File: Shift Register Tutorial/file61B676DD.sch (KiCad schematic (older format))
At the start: 7 parts, among them Q301 2N3904, SW301 SW_Push

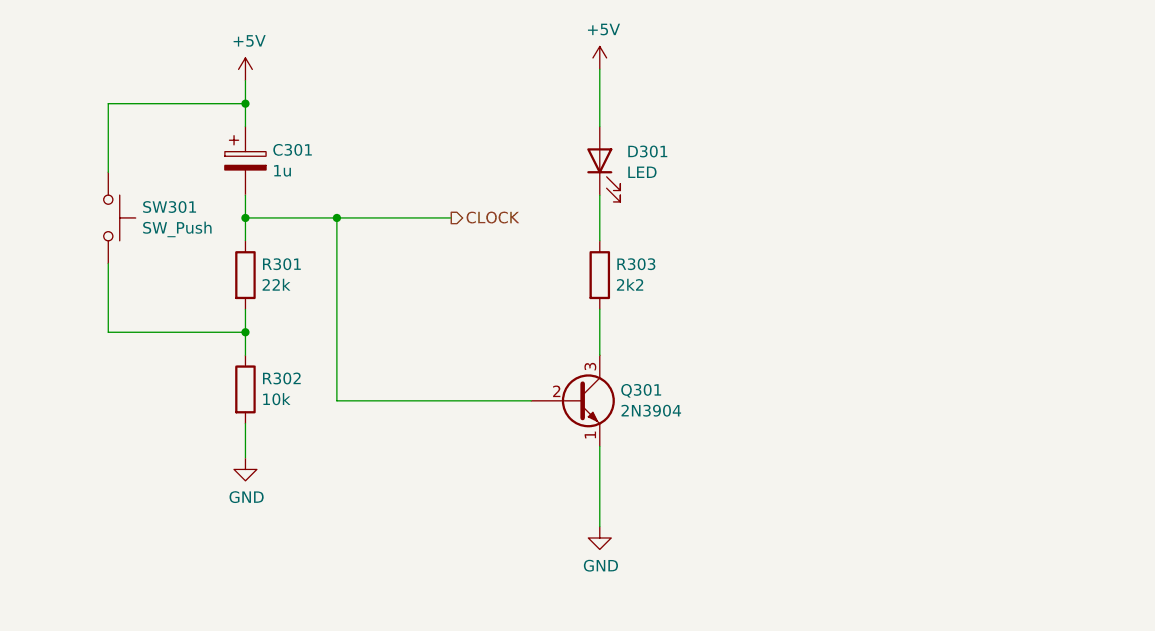
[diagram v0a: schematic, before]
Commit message: Fix shift register tutorial (#11)
I had forgotten how NPN transistors worked, which resulted in the push buttons not affecting their target pins. Remove the transistors & indicator LEDs, and shrink the board.
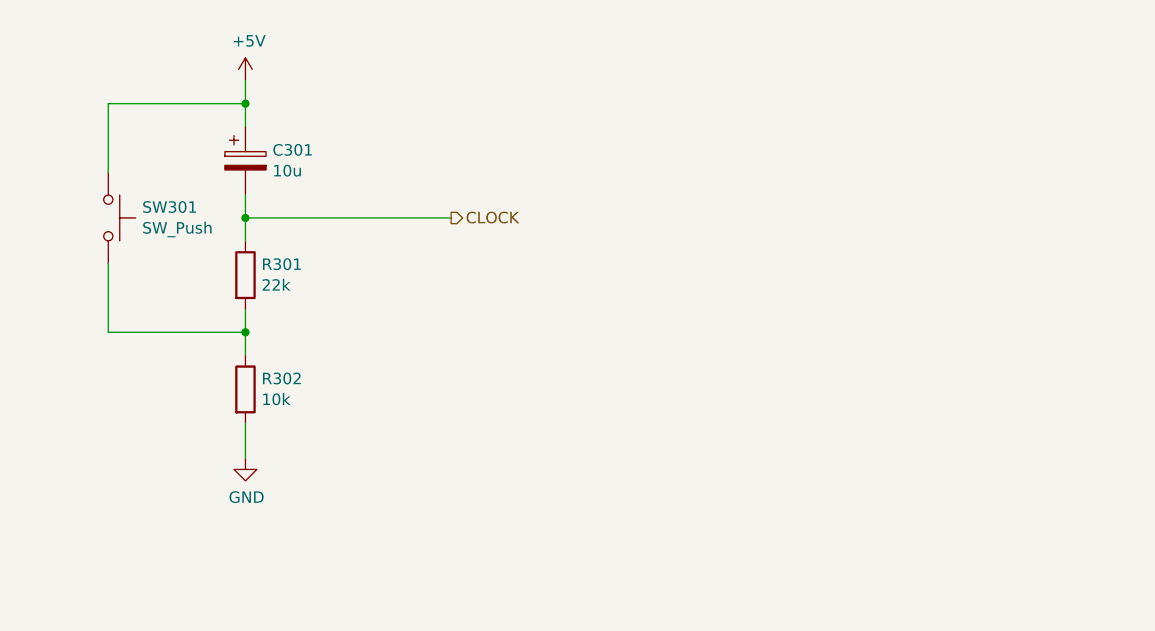
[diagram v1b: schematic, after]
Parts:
- removed D301: LED, LED_THT:LED_D5.0mm, symbol Device:LED
- removed Q301: 2N3904, Package_TO_SOT_THT:TO-92_Inline_Wide, symbol Transistor_BJT:2N3904
- removed R303: 2k2, Resistor_THT:R_Axial_DIN0207_L6.3mm_D2.5mm_P7.62mm_Horizontal, symbol Device:R
- C301: value 1u -> 10u
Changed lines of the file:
@@
 AR Path="/61B676DE/61B6A311" Ref="C301"  Part="1"
 F 0 "C301" H 2768 1746 50  0000 L CNN
-F 1 "1u" H 2768 1655 50  0000 L CNN
+F 1 "10u" H 2768 1655 50  0000 L CNN
 F 2 "Capacitor_THT:CP_Radial_D4.0mm_P2.00mm" H 2688 1550 50  0001 C CNN
 F 3 "~" H 2650 1700 50  0001 C CNN
@@
 Text HLabel 3550 1950 2    50   Output ~ 0
 CLOCK
-Wire Wire Line
-	2650 1950 3050 1950
 Connection ~ 2650 1950
 Wire Wire Line
 	2650 1950 2650 2050
-$Comp
-L Transistor_BJT:2N3904 Q?
-U 1 1 61B6A339
-P 4100 2750
-AR Path="/61B52EB5/61B6A339" Ref="Q?"  Part="1"
-AR Path="/61B676DE/61B6A339" Ref="Q301"  Part="1"
-F 0 "Q301" H 4290 2796 50  0000 L CNN
-F 1 "2N3904" H 4290 2705 50  0000 L CNN
-F 2 "Package_TO_SOT_THT:TO-92_Inline_Wide" H 4300 2675 50  0001 L CIN
-F 3 "https://www.onsemi.com/pub/Collateral/2N3903-D.PDF" H 4100 2750 50  0001 L CNN
-	1    4100 2750
-	1    0    0    -1
-$EndComp
 Wire Wire Line
-	3050 1950 3050 2750
-Wire Wire Line
-	3050 2750 3900 2750
-Connection ~ 3050 1950
-Wire Wire Line
-	3050 1950 3550 1950
-$Comp
-L power:GND #PWR?
-U 1 1 61B6A343
-P 4200 3300
-AR Path="/61B52EB5/61B6A343" Ref="#PWR?"  Part="1"
-AR Path="/61B676DE/61B6A343" Ref="#PWR0304"  Part="1"
-F 0 "#PWR0304" H 4200 3050 50  0001 C CNN
-F 1 "GND" H 4205 3127 50  0000 C CNN
-F 2 "" H 4200 3300 50  0001 C CNN
-F 3 "" H 4200 3300 50  0001 C CNN
-	1    4200 3300
-	1    0    0    -1
-$EndComp
-Wire Wire Line
-	4200 2950 4200 3300
-$Comp
-L Device:R R?
-U 1 1 61B6A34A
-P 4200 2200
-AR Path="/61B52EB5/61B6A34A" Ref="R?"  Part="1"
-AR Path="/61B676DE/61B6A34A" Ref="R303"  Part="1"
-F 0 "R303" H 4270 2246 50  0000 L CNN
-F 1 "2k2" H 4270 2155 50  0000 L CNN
-F 2 "Resistor_THT:R_Axial_DIN0207_L6.3mm_D2.5mm_P7.62mm_Horizontal" V 4130 2200 50  0001 C CNN
-F 3 "~" H 4200 2200 50  0001 C CNN
-	1    4200 2200
-	1    0    0    -1
-$EndComp
-$Comp
-L Device:LED D?
-U 1 1 61B6A350
-P 4200 1700
-AR Path="/61B52EB5/61B6A350" Ref="D?"  Part="1"
-AR Path="/61B676DE/61B6A350" Ref="D301"  Part="1"
-F 0 "D301" V 4239 1582 50  0000 R CNN
-F 1 "LED" V 4148 1582 50  0000 R CNN
-F 2 "LED_THT:LED_D5.0mm" H 4200 1700 50  0001 C CNN
-F 3 "~" H 4200 1700 50  0001 C CNN
-	1    4200 1700
-	0    -1   -1   0
-$EndComp
-$Comp
-L power:+5V #PWR?
-U 1 1 61B6A356
-P 4200 1300
-AR Path="/61B52EB5/61B6A356" Ref="#PWR?"  Part="1"
-AR Path="/61B676DE/61B6A356" Ref="#PWR0303"  Part="1"
-F 0 "#PWR0303" H 4200 1150 50  0001 C CNN
-F 1 "+5V" H 4215 1473 50  0000 C CNN
-F 2 "" H 4200 1300 50  0001 C CNN
-F 3 "" H 4200 1300 50  0001 C CNN
-	1    4200 1300
-	1    0    0    -1
-$EndComp
-Wire Wire Line
-	4200 1300 4200 1550
-Wire Wire Line
-	4200 1850 4200 2050
-Wire Wire Line
-	4200 2350 4200 2550
+	2650 1950 3550 1950
 $EndSCHEMATC

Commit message: Another attempt at the Shift Registers (#12)
It appears that clock pins are very finicky about debouncing. Switch to using a 555 monostable for this purpose, and remove debounce from the other pins. The 'data' pin only matters on the clock edge, and the 'reset' pin is idempotent.
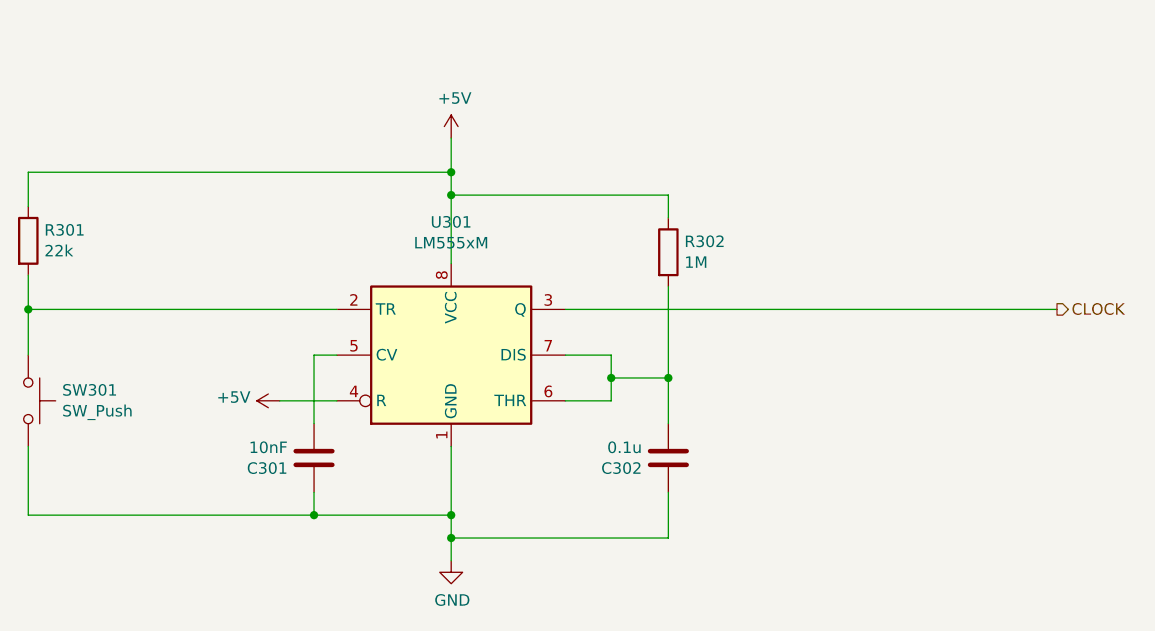
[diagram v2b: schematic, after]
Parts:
- removed C301: 10u, Capacitor_THT:CP_Radial_D4.0mm_P2.00mm, symbol Device:CP
- added C301: 10nF, Capacitor_THT:C_Disc_D3.0mm_W2.0mm_P2.50mm, symbol Device:C
- added C302: 0.1u, Capacitor_THT:C_Disc_D4.7mm_W2.5mm_P5.00mm, symbol Device:C
- added U301: LM555xM, Package_DIP:DIP-8_W7.62mm_Socket, symbol Timer:LM555xM
- R302: value 10k -> 1M
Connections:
- net +5V: now also R301.1, R302.1, U301.4 (R), U301.8 (VCC); no longer SW301.1
- net CLOCK: now also U301.3 (Q); no longer R301.1
- net GND: now also SW301.2, C301.2, C302.1, U301.1 (GND); no longer R302.2
- new net: R301.2, SW301.1, U301.2 (TR)
- new net: C301.1, U301.5 (CV)
- new net: C302.2, R302.2, U301.6 (THR), U301.7 (DIS)
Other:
- moved on the sheet: SW301
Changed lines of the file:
@@
 $EndDescr
-$Comp
-L Device:R R?
-U 1 1 61B6A305
-P 2650 2700
-AR Path="/61B52EB5/61B6A305" Ref="R?"  Part="1"
-AR Path="/61B676DE/61B6A305" Ref="R302"  Part="1"
-F 0 "R302" H 2720 2746 50  0000 L CNN
-F 1 "10k" H 2720 2655 50  0000 L CNN
-F 2 "Resistor_THT:R_Axial_DIN0207_L6.3mm_D2.5mm_P7.62mm_Horizontal" V 2580 2700 50  0001 C CNN
-F 3 "~" H 2650 2700 50  0001 C CNN
-	1    2650 2700
-	1    0    0    -1
-$EndComp
-$Comp
-L Device:R R?
-U 1 1 61B6A30B
-P 2650 2200
-AR Path="/61B52EB5/61B6A30B" Ref="R?"  Part="1"
-AR Path="/61B676DE/61B6A30B" Ref="R301"  Part="1"
-F 0 "R301" H 2720 2246 50  0000 L CNN
-F 1 "22k" H 2720 2155 50  0000 L CNN
-F 2 "Resistor_THT:R_Axial_DIN0207_L6.3mm_D2.5mm_P7.62mm_Horizontal" V 2580 2200 50  0001 C CNN
-F 3 "~" H 2650 2200 50  0001 C CNN
-	1    2650 2200
-	1    0    0    -1
-$EndComp
-$Comp
-L Device:CP C?
-U 1 1 61B6A311
-P 2650 1700
-AR Path="/61B52EB5/61B6A311" Ref="C?"  Part="1"
-AR Path="/61B676DE/61B6A311" Ref="C301"  Part="1"
-F 0 "C301" H 2768 1746 50  0000 L CNN
-F 1 "10u" H 2768 1655 50  0000 L CNN
-F 2 "Capacitor_THT:CP_Radial_D4.0mm_P2.00mm" H 2688 1550 50  0001 C CNN
-F 3 "~" H 2650 1700 50  0001 C CNN
-	1    2650 1700
-	1    0    0    -1
-$EndComp
 $Comp
 L power:+5V #PWR?
 U 1 1 61B6A317
-P 2650 1350
+P 3550 1600
 AR Path="/61B52EB5/61B6A317" Ref="#PWR?"  Part="1"
-AR Path="/61B676DE/61B6A317" Ref="#PWR0301"  Part="1"
-F 0 "#PWR0301" H 2650 1200 50  0001 C CNN
-F 1 "+5V" H 2665 1523 50  0000 C CNN
-F 2 "" H 2650 1350 50  0001 C CNN
-F 3 "" H 2650 1350 50  0001 C CNN
-	1    2650 1350
+AR Path="/61B676DE/61B6A317" Ref="#PWR0302"  Part="1"
+F 0 "#PWR0302" H 3550 1450 50  0001 C CNN
+F 1 "+5V" H 3565 1773 50  0000 C CNN
+F 2 "" H 3550 1600 50  0001 C CNN
+F 3 "" H 3550 1600 50  0001 C CNN
+	1    3550 1600
 	1    0    0    -1
 $EndComp
@@
 L power:GND #PWR?
 U 1 1 61B6A31D
-P 2650 3000
+P 3550 3450
 AR Path="/61B52EB5/61B6A31D" Ref="#PWR?"  Part="1"
-AR Path="/61B676DE/61B6A31D" Ref="#PWR0302"  Part="1"
-F 0 "#PWR0302" H 2650 2750 50  0001 C CNN
-F 1 "GND" H 2655 2827 50  0000 C CNN
-F 2 "" H 2650 3000 50  0001 C CNN
-F 3 "" H 2650 3000 50  0001 C CNN
-	1    2650 3000
+AR Path="/61B676DE/61B6A31D" Ref="#PWR0303"  Part="1"
+F 0 "#PWR0303" H 3550 3200 50  0001 C CNN
+F 1 "GND" H 3555 3277 50  0000 C CNN
+F 2 "" H 3550 3450 50  0001 C CNN
+F 3 "" H 3550 3450 50  0001 C CNN
+	1    3550 3450
+	1    0    0    -1
+$EndComp
+$Comp
+L Switch:SW_Push SW?
+U 1 1 61B6A327
+P 1700 2750
+AR Path="/61B52EB5/61B6A327" Ref="SW?"  Part="1"
+AR Path="/61B676DE/61B6A327" Ref="SW301"  Part="1"
+F 0 "SW301" V 1654 2898 50  0000 L CNN
+F 1 "SW_Push" V 1745 2898 50  0000 L CNN
+F 2 "Button_Switch_THT:SW_PUSH_6mm_H4.3mm" H 1700 2950 50  0001 C CNN
+F 3 "~" H 1700 2950 50  0001 C CNN
+	1    1700 2750
+	0    1    1    0
+$EndComp
+Wire Wire Line
+	1700 2950 1700 3250
+Text HLabel 6200 2350 2    50   Output ~ 0
+CLOCK
+$Comp
+L Timer:LM555xM U301
+U 1 1 61C83383
+P 3550 2550
+F 0 "U301" H 3550 3131 50  0000 C CNN
+F 1 "LM555xM" H 3550 3040 50  0000 C CNN
+F 2 "Package_DIP:DIP-8_W7.62mm_Socket" H 4400 2150 50  0001 C CNN
+F 3 "http://www.ti.com/lit/ds/symlink/lm555.pdf" H 4400 2150 50  0001 C CNN
+	1    3550 2550
 	1    0    0    -1
 $EndComp
 Wire Wire Line
-	2650 1350 2650 1450
+	3550 1600 3550 1750
 Wire Wire Line
-	2650 1850 2650 1950
-Wire Wire Line
-	2650 2350 2650 2450
-Wire Wire Line
-	2650 2850 2650 3000
+	3550 2950 3550 3250
 $Comp
-L Switch:SW_Push SW?
-U 1 1 61B6A327
-P 2050 1950
-AR Path="/61B52EB5/61B6A327" Ref="SW?"  Part="1"
-AR Path="/61B676DE/61B6A327" Ref="SW301"  Part="1"
-F 0 "SW301" V 2004 2098 50  0000 L CNN
-F 1 "SW_Push" V 2095 2098 50  0000 L CNN
-F 2 "Button_Switch_THT:SW_PUSH_6mm_H4.3mm" H 2050 2150 50  0001 C CNN
-F 3 "~" H 2050 2150 50  0001 C CNN
-	1    2050 1950
-	0    1    1    0
+L power:+5V #PWR0301
+U 1 1 61C85217
+P 2800 2750
+F 0 "#PWR0301" H 2800 2600 50  0001 C CNN
+F 1 "+5V" V 2815 2878 50  0000 L CNN
+F 2 "" H 2800 2750 50  0001 C CNN
+F 3 "" H 2800 2750 50  0001 C CNN
+	1    2800 2750
+	0    -1   -1   0
 $EndComp
 Wire Wire Line
-	2050 2150 2050 2450
+	2800 2750 3050 2750
 Wire Wire Line
-	2050 2450 2650 2450
-Connection ~ 2650 2450
+	1700 3250 2950 3250
+Connection ~ 3550 3250
 Wire Wire Line
-	2650 2450 2650 2550
+	3550 3250 3550 3350
 Wire Wire Line
-	2050 1750 2050 1450
+	1700 2550 1700 2350
 Wire Wire Line
-	2050 1450 2650 1450
-Connection ~ 2650 1450
+	1700 2350 3050 2350
+$Comp
+L Device:R R301
+U 1 1 61C8660C
+P 1700 2050
+F 0 "R301" H 1770 2096 50  0000 L CNN
+F 1 "22k" H 1770 2005 50  0000 L CNN
+F 2 "Resistor_THT:R_Axial_DIN0207_L6.3mm_D2.5mm_P7.62mm_Horizontal" V 1630 2050 50  0001 C CNN
+F 3 "~" H 1700 2050 50  0001 C CNN
+	1    1700 2050
+	1    0    0    -1
+$EndComp
 Wire Wire Line
-	2650 1450 2650 1550
-Text HLabel 3550 1950 2    50   Output ~ 0
-CLOCK
-Connection ~ 2650 1950
+	1700 1900 1700 1750
 Wire Wire Line
-	2650 1950 2650 2050
+	1700 1750 3550 1750
+Connection ~ 3550 1750
 Wire Wire Line
-	2650 1950 3550 1950
+	3550 1750 3550 1850
+Wire Wire Line
+	1700 2200 1700 2350
+Connection ~ 1700 2350
+Wire Wire Line
+	4050 2350 6200 2350
+$Comp
+L Device:C C301
+U 1 1 61C8755C
+P 2950 3000
+F 0 "C301" H 2835 2954 50  0000 R CNN
+F 1 "10nF" H 2835 3045 50  0000 R CNN
+F 2 "Capacitor_THT:C_Disc_D3.0mm_W2.0mm_P2.50mm" H 2988 2850 50  0001 C CNN
+F 3 "~" H 2950 3000 50  0001 C CNN
+	1    2950 3000
+	1    0    0    -1
+$EndComp
+Wire Wire Line
+	2950 2850 2950 2550
+Wire Wire Line
+	2950 2550 3050 2550
+Wire Wire Line
+	2950 3150 2950 3250
+Connection ~ 2950 3250
+Wire Wire Line
+	2950 3250 3550 3250
+Wire Wire Line
+	4050 2550 4250 2550
+Wire Wire Line
+	4250 2550 4250 2650
+Wire Wire Line
+	4250 2750 4050 2750
+$Comp
+L Device:R R302
+U 1 1 61C89931
+P 4500 2100
+F 0 "R302" H 4570 2146 50  0000 L CNN
+F 1 "1M" H 4570 2055 50  0000 L CNN
+F 2 "Resistor_THT:R_Axial_DIN0207_L6.3mm_D2.5mm_P7.62mm_Horizontal" V 4430 2100 50  0001 C CNN
+F 3 "~" H 4500 2100 50  0001 C CNN
+	1    4500 2100
+	1    0    0    -1
+$EndComp
+$Comp
+L Device:C C302
+U 1 1 61C89DC7
+P 4500 3000
+F 0 "C302" H 4615 3046 50  0000 L CNN
+F 1 "0.1u" H 4615 2955 50  0000 L CNN
+F 2 "Capacitor_THT:C_Disc_D4.7mm_W2.5mm_P5.00mm" H 4538 2850 50  0001 C CNN
+F 3 "~" H 4500 3000 50  0001 C CNN
+	1    4500 3000
+	-1   0    0    1
+$EndComp
+Wire Wire Line
+	4500 2250 4500 2650
+Wire Wire Line
+	3550 3350 4500 3350
+Wire Wire Line
+	4500 3350 4500 3150
+Connection ~ 3550 3350
+Wire Wire Line
+	3550 3350 3550 3450
+Wire Wire Line
+	4250 2650 4500 2650
+Connection ~ 4250 2650
+Wire Wire Line
+	4250 2650 4250 2750
+Connection ~ 4500 2650
+Wire Wire Line
+	4500 2650 4500 2850
+Wire Wire Line
+	4500 1950 4500 1850
+Wire Wire Line
+	4500 1850 3550 1850
+Connection ~ 3550 1850
+Wire Wire Line
+	3550 1850 3550 2150
 $EndSCHEMATC
